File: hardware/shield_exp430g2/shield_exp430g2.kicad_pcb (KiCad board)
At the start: 2 copper layers, 58.7 x 51.2 mm, 46 parts, among them J1 Digital, J10 Conn_01x02_Male, J11 Conn_01x02_Male, J12 Conn_01x02_Male, J13 Conn_01x02_Male, J14 Conn_01x04_Male, J15 Conn_01x02_Male, J16 Conn_01x02_Male, J17 Conn_01x02_Male, J18 Conn_01x02_Male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

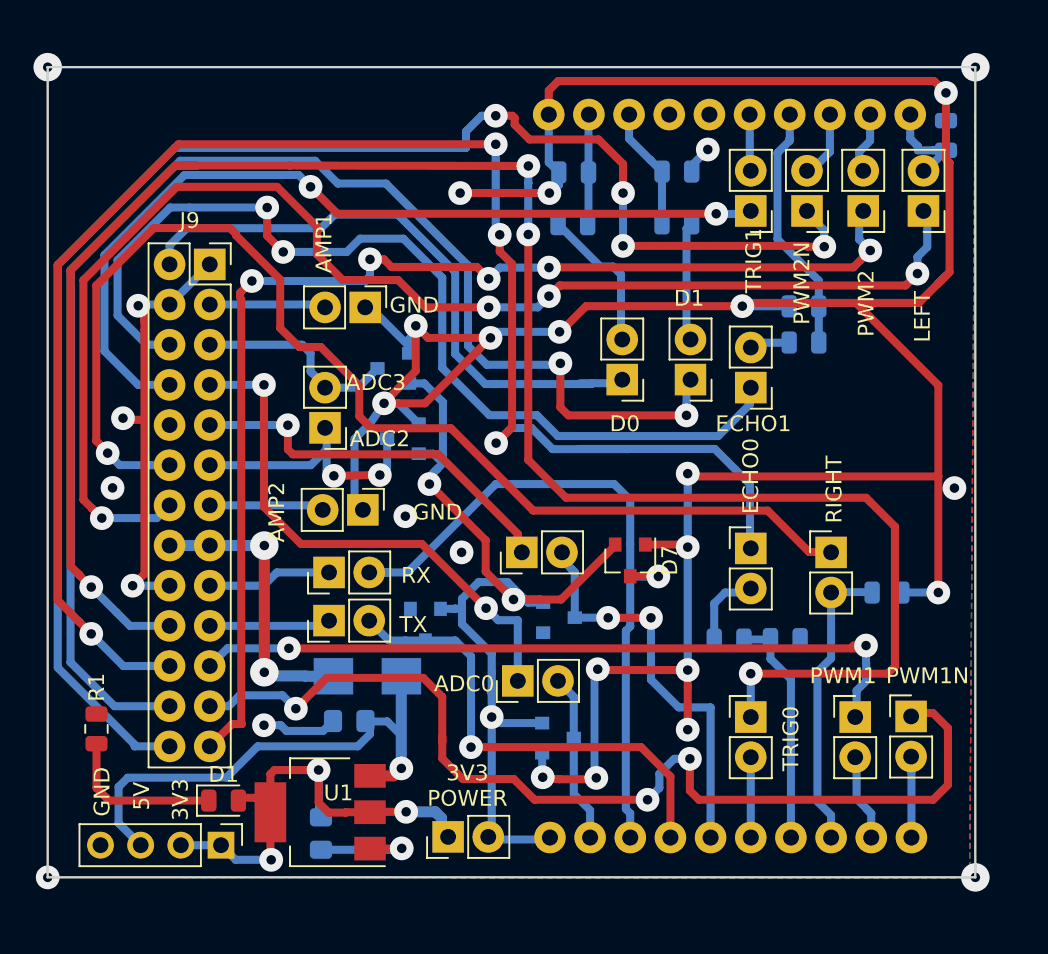
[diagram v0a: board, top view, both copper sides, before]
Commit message: Change 26 via connector
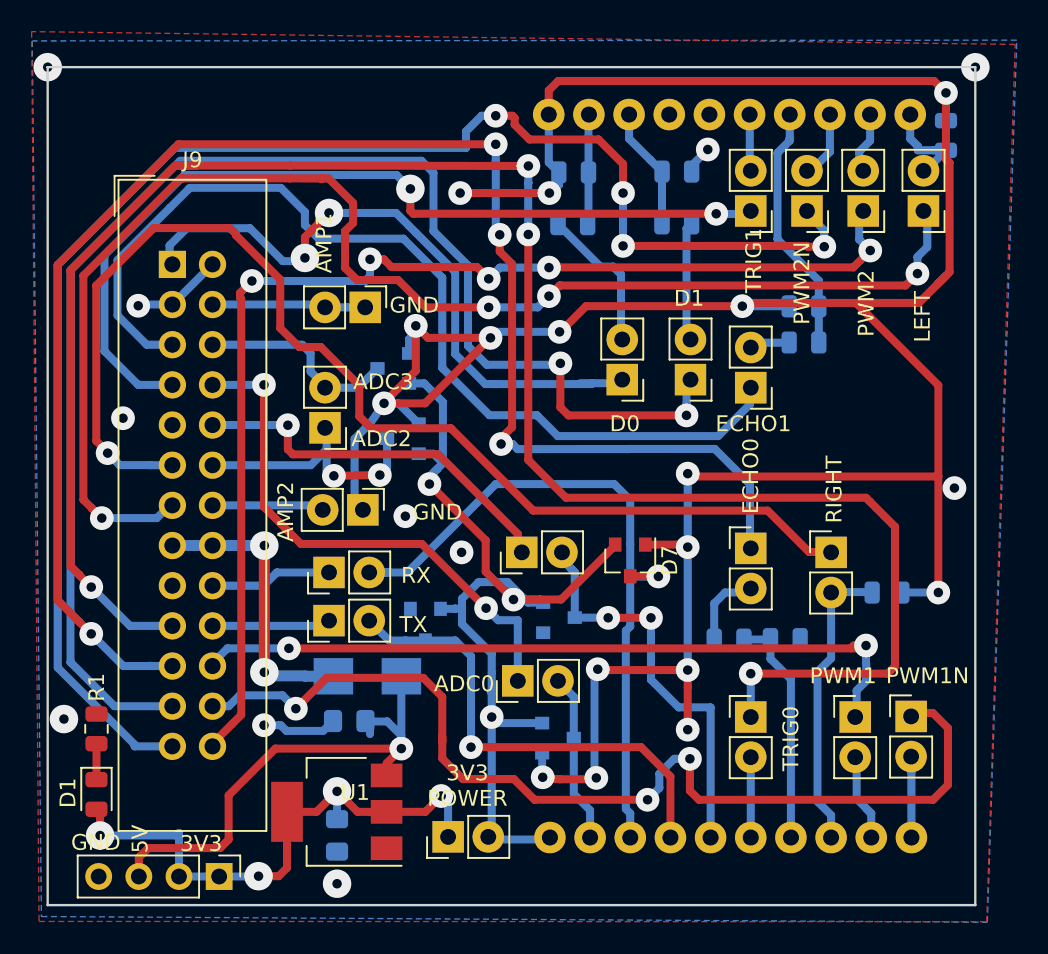
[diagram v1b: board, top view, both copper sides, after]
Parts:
- J9: footprint Connector_PinSocket_2.54mm:PinSocket_2x13_P2.54mm_Vertical -> Connector_IDC:IDC-Header_2x13_P2.54mm_Vertical
- R10, R11, R3, R5, R8, R9: value 20K -> 15k
- moved D1 8.05 mm to (112.8, 121.1), turned to 270 degrees
- moved J9 2.36 mm to (117.6, 87.6)
- moved J14 1.99 mm to (120.6, 126.3)
- moved U1 1.05 mm to (128.0, 122.2)
- moved C2 1.02 mm to (128.0, 123.7)
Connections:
- J4 pad 1: GND -> AMP1
- J9 pad 1: GND -> D0
- J9 pad 10: Net-(J9-Pad10) -> ADC1
- J9 pad 11: ADC2 -> R_TCRT
- J9 pad 12: R_TCRT -> ADC2
- J9 pad 13: AMP2 -> L_TCRT
- J9 pad 14: L_TCRT -> AMP2
- J9 pad 17: TXB -> GND
- J9 pad 18: GND -> TXB
- J9 pad 19: RXB -> Trig0
- J9 pad 2: D0 -> GND
- J9 pad 20: Trig0 -> RXB
- J9 pad 21: PWM1 -> Echo0
- J9 pad 22: Echo0 -> PWM1
- J9 pad 23: PWM1N -> D1
- J9 pad 24: D1 -> PWM1N
- J9 pad 25: PWM2 -> PWM2N
- J9 pad 26: PWM2N -> PWM2
- J9 pad 3: AMP1 -> GND
- J9 pad 4: GND -> AMP1
- J9 pad 5: ADC3 -> Echo1
- J9 pad 6: Echo1 -> ADC3
- J9 pad 7: ADC0 -> Trig1
- J9 pad 8: Trig1 -> ADC0
- J9 pad 9: ADC1 -> Net-(J9-Pad9)
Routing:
- net GND: track 238.9 -> 205.8 mm, vias 26 -> 25
- net Net-(D1-Pad1): track 10.2 -> 2.27 mm
- net Net-(C2-Pad1): track 34.3 -> 37.8 mm, vias 3 -> 4
- net L_TCRT: track 84.5 -> 87.3 mm
- net +5V: track 34.8 -> 32.1 mm
- net D0: track 39.2 -> 41.8 mm, vias 0 -> 2
- net D1: track 87.5 -> 89.6 mm
- net AMP1: track 7.42 -> 9.28 mm
- net Echo0: track 111.5 -> 110.4 mm
- net Trig1: track 55.0 -> 55.8 mm
- net Echo1: track 62.2 -> 62.0 mm, vias 2 -> 0
- net (no net): vias 4 -> 2
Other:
- board size 58.7 x 51.2 mm -> 58.7 x 53 mm

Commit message: Added board info
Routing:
- net (no net): vias 2 -> 0
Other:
- board text added: "Shield EXP430G2 Prof. Renan Augusto Starke"
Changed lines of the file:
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@@
   (general
     (thickness 1.6)
-    (drawings 32)
-    (tracks 660)
+    (drawings 33)
+    (tracks 658)
     (zones 0)
     (modules 46)
@@
     (visible_elements FFFFFF7F)
     (pcbplotparams
-      (layerselection 0x00030_80000001)
+      (layerselection 0x01030_ffffffff)
       (usegerberextensions false)
       (usegerberattributes false)
@@
       (outputformat 1)
       (mirror false)
-      (drillshape 1)
+      (drillshape 0)
       (scaleselection 1)
-      (outputdirectory ""))
+      (outputdirectory "fabric/"))
   )
   (net 0 "")
@@
     )
   )
+  (gr_text "Shield EXP430G2\nProf. Renan Augusto Starke" (at 121.92 77.465) (layer F.SilkS)
+    (effects (font (size 1 1) (thickness 0.1)))
+  )
   (target plus (at 168.3766 75.1078) (size 5) (width 0.15) (layer Edge.Cuts))
   (target plus (at 167.061621 101.72611) (size 2) (width 0.15) (layer Edge.Cuts))
@@
   (gr_line (start 168.3766 128.1) (end 168.3766 75.1078) (layer Edge.Cuts) (width 0.15))
   (gr_line (start 109.7153 75.1078) (end 109.7153 128.1) (angle 90) (layer Edge.Cuts) (width 0.15))
-  (via (at 109.71784 75.1078) (size 1.8) (drill 0.6) (layers F.Cu B.Cu) (net 0))
-  (via (at 168.38168 75.11288) (size 1.8) (drill 0.6) (layers F.Cu B.Cu) (net 0))
   (via (at 132.08 118.2) (size 1.5) (drill 0.6) (layers F.Cu B.Cu) (net 1))
   (segment (start 132.08 113.6306) (end 132.0837 113.6269) (width 0.508) (layer B.Cu) (net 1))
@@
   (via (at 110.744 116.332) (size 1.8) (drill 0.6) (layers F.Cu B.Cu) (net 2))
   (via (at 135.89 105.791) (size 1.5) (drill 0.6) (layers F.Cu B.Cu) (net 2))
-  (via (at 132.9944 91.4654) (size 1.5) (drill 0.6) (layers F.Cu B.Cu) (net 2) (status 1000000))
+  (via (at 132.9944 91.4654) (size 1.5) (drill 0.6) (layers F.Cu B.Cu) (net 2))
   (via (at 137.795 116.205) (size 1.5) (drill 0.6) (layers F.Cu B.Cu) (net 3))
   (segment (start 138.1785 116.5885) (end 137.795 116.205) (width 0.508) (layer B.Cu) (net 3))
